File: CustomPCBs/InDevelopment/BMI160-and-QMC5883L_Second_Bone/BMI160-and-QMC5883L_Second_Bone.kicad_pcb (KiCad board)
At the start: 4 copper layers, 6.7 x 13.4 mm, 14 parts, among them J1 Conn_01x04_MountingPin, J2 Conn_01x04_MountingPin, U1 BMI160, U2 QMC5883L

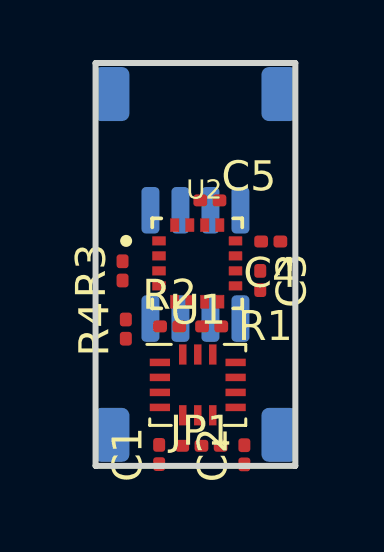
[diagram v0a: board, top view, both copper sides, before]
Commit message: BMI160+mag board finished, fixed CS on ICM-20948
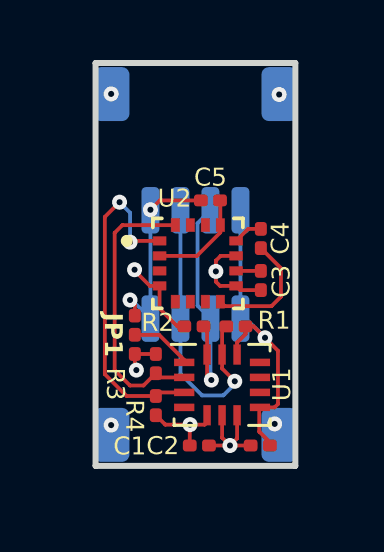
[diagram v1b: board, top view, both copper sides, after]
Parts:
- moved JP1 4.31 mm to (109.3, 86.7), turned to -90 degrees
- moved R3 3.28 mm to (110.0, 87.6), turned to -90 degrees
- moved R4 2.74 mm to (110.0, 89.0)
- moved C1 1.37 mm to (111.5, 90.4), turned to 180 degrees
- moved R1 0.81 mm to (112.7, 86.4)
- moved R2 0.81 mm to (111.3, 86.4)
- moved U1 0.81 mm to (112.2, 88.3)
- moved C2 0.61 mm to (113.5, 90.4), turned to 180 degrees
- moved C4 0.34 mm to (113.5, 83.5), turned to 90 degrees
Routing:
- net +3.3V: track 0.00 -> 18.0 mm, vias 0 -> 4
- net GND: track 0.00 -> 14.7 mm, vias 0 -> 8
- net Net-(U1-ASCx): track 0.00 -> 11.4 mm, vias 0 -> 2
- net SCL: track 0.00 -> 9.67 mm, vias 0 -> 1
- net Net-(U1-ASDx): track 0.00 -> 9.44 mm
- net SDA: track 0.00 -> 7.75 mm, vias 0 -> 1
- net Net-(U2-SETP): track 0.00 -> 4.11 mm
- net Net-(U2-VDD): track 0.00 -> 3.42 mm
- net Net-(JP1-C): track 0.00 -> 2.07 mm
- net Net-(U2-SETC): track 0.00 -> 1.02 mm
- net Net-(U2-C1): track 0.00 -> 0.83 mm
- added copper zone on In1.Cu, net +3.3V
- added copper zone on In2.Cu, net GND
